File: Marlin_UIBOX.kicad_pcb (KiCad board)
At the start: 2 copper layers, 45 x 40 mm, 11 parts, among them J1 EXP1, J2 EXP2, J3 12864OLED_SPI, J4 SD_CARD, J5 ROT_ENCODER, Q1 2N3904

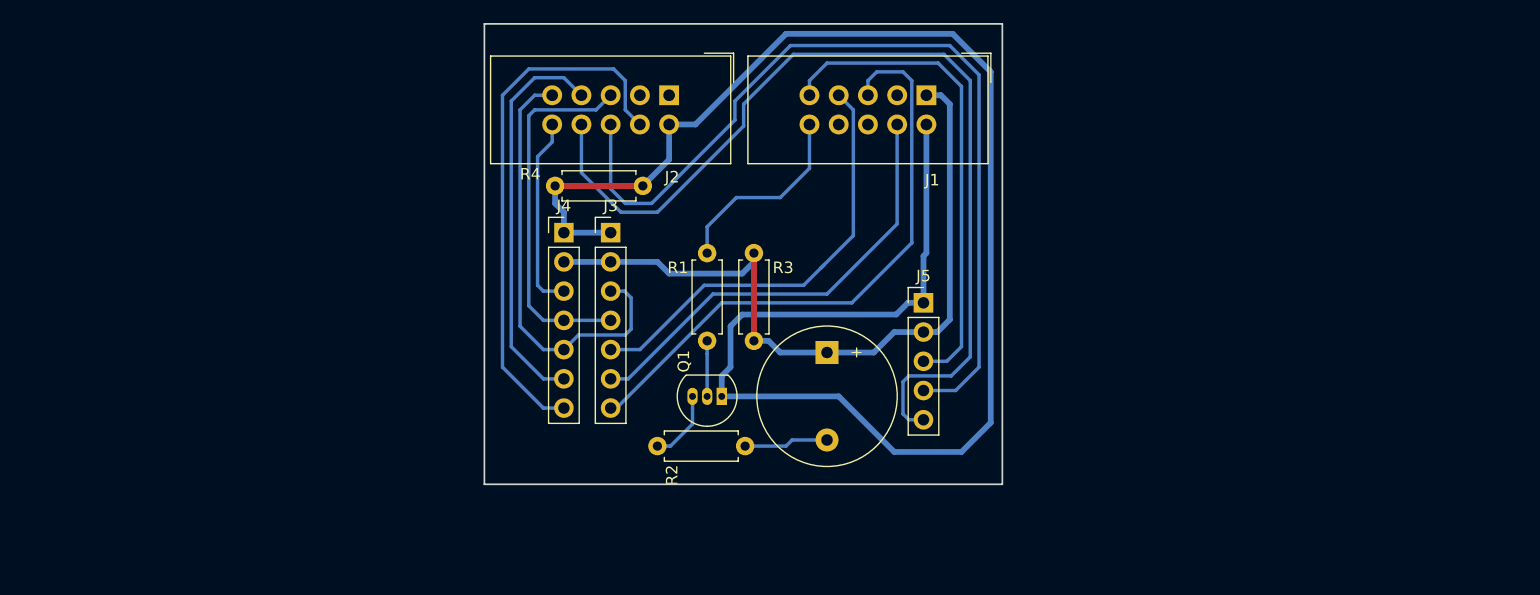
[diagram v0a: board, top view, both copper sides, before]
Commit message: PCB ver2 full board to board connections
* Complete re-do PCB to have PCB to PCB connectors no wire needed
* Went with 2 layer PCB instead of trying to make single layer...
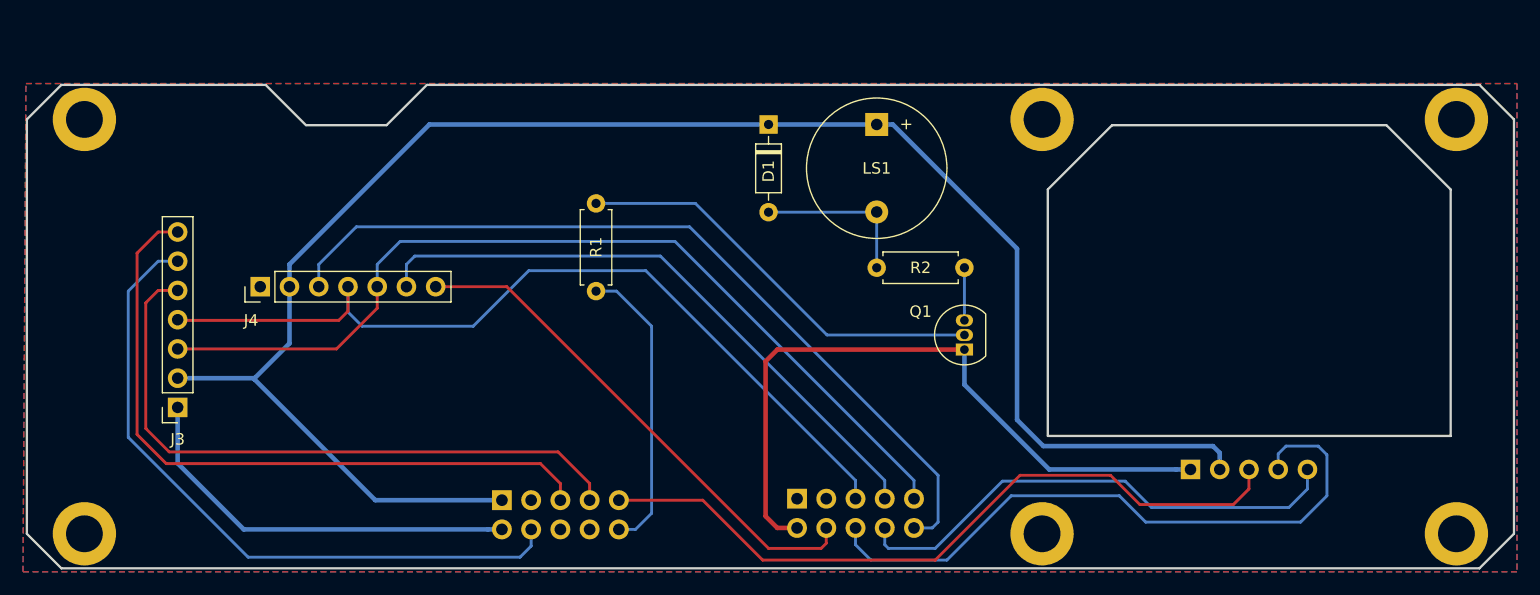
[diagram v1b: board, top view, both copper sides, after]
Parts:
- removed R3, R4: 0K, Resistors_ThroughHole:R_Axial_DIN0207_L6.3mm_D2.5mm_P7.62mm_Horizontal
- added D1: D, Diode_THT:D_DO-35_SOD27_P7.62mm_Horizontal, F.Cu at (154.7, 78.7)
- added REF**: MountingHole_3.2mm_M3_ISO14580_Pad, Mounting_Holes:MountingHole_3.2mm_M3_ISO14580_Pad, F.Cu at (214.4, 114.3)
- added REF**: MountingHole_3.2mm_M3_ISO14580_Pad, Mounting_Holes:MountingHole_3.2mm_M3_ISO14580_Pad, F.Cu at (214.4, 78.3)
- added REF**: MountingHole_3.2mm_M3_ISO14580_Pad, Mounting_Holes:MountingHole_3.2mm_M3_ISO14580_Pad, F.Cu at (178.4, 78.3)
- added REF**: MountingHole_3.2mm_M3_ISO14580_Pad, Mounting_Holes:MountingHole_3.2mm_M3_ISO14580_Pad, F.Cu at (178.4, 114.3)
- added REF**: MountingHole_3.2mm_M3_ISO14580_Pad, Mounting_Holes:MountingHole_3.2mm_M3_ISO14580_Pad, F.Cu at (95.2, 114.3)
- added REF**: MountingHole_3.2mm_M3_ISO14580_Pad, Mounting_Holes:MountingHole_3.2mm_M3_ISO14580_Pad, F.Cu at (95.2, 78.3)
- J1, J2: moved to B.Cu
- J3: footprint Pin_Headers:Pin_Header_Straight_1x07_Pitch2.54mm -> Connector_PinSocket_2.54mm:PinSocket_1x07_P2.54mm_Vertical
- J5: footprint Pin_Headers:Pin_Header_Straight_1x05_Pitch2.54mm -> Connector_PinSocket_2.54mm:PinSocket_1x05_P2.54mm_Vertical; moved to B.Cu
- LS1: footprint Buzzers_Beepers:Buzzer_12x9.5RM7.6 -> Buzzer_Beeper:Buzzer_12x9.5RM7.6
- Q1: footprint TO_SOT_Packages_THT:TO-92_Inline_Narrow_Oval -> Package_TO_SOT_THT:TO-92_Inline
- R1, R2: footprint Resistors_ThroughHole:R_Axial_DIN0207_L6.3mm_D2.5mm_P7.62mm_Horizontal -> Resistor_THT:R_Axial_DIN0207_L6.3mm_D2.5mm_P7.62mm_Horizontal
- moved J1 51.0 mm to (131.5, 111.4)
- moved J3 40.6 mm to (103.3, 103.3), turned to 180 degrees
- moved J2 36.8 mm to (157.2, 111.3)
- moved J5 27.3 mm to (191.3, 108.7), turned to 270 degrees
- moved J4 26.8 mm to (110.5, 92.8), turned to 90 degrees
- moved Q1 21.5 mm to (171.7, 98.3), turned to 90 degrees
- moved LS1 20.3 mm to (164.1, 78.7)
- moved R2 19.3 mm to (164.1, 91.2), turned to 0 degrees
- moved R1 10.2 mm to (139.7, 93.2), turned to 90 degrees
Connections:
- J1 pad 3: (no net) -> Net-(J1-Pad3)
- J1 pad 6: (no net) -> Net-(J1-Pad6)
- J1 pad 8: (no net) -> Net-(J1-Pad8)
- J2 pad 1: (no net) -> Net-(J2-Pad1)
- J2 pad 3: (no net) -> Net-(J2-Pad3)
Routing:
- net VCC: track 65.9 -> 151.6 mm
- net GND: track 151.4 -> 95.5 mm
- net /MISO: track 17.0 -> 72.4 mm
- net /MOSI: track 32.0 -> 75.2 mm
- net /SCK: track 38.1 -> 80.3 mm
- net /BT_EN2: track 82.7 -> 44.0 mm
- net Net-(Q1-Pad2): track 4.83 -> 36.7 mm
- net /BT_SW: track 42.4 -> 63.3 mm
- net /LCD_DC: track 39.1 -> 59.2 mm
- net /BT_EN1: track 76.9 -> 56.9 mm
- net /SD_SS: track 34.6 -> 53.5 mm
- net /LCD_RES: track 38.3 -> 56.1 mm
- net /BEEPER: track 17.1 -> 25.8 mm
- net /LCD_CS: track 51.9 -> 60.0 mm
- net Net-(D1-Pad2): track 7.33 -> 14.3 mm
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- added copper zone on B.Cu, net GND
- added copper zone on F.Cu, net GND
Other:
- board size 45 x 40 mm -> 129.2 x 42 mm
- net class Default: trace_width 0.3 -> 0.25
- net class POWER removed
- net class Power added: clearance 0.2, trace_width 0.4, via_dia 0.8, via_drill 0.4

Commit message: Move parts to fit both Replicator 1 and 2
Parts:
- moved D1 28.6 mm to (126.5, 83.3), turned to 0 degrees
- moved R2 9.76 mm to (171.7, 85.1), turned to 270 degrees
- moved LS1 6.19 mm to (162.1, 84.6)
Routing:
- net Net-(D1-Pad2): track 14.3 -> 45.1 mm
- net VCC: track 151.6 -> 156.3 mm
- net Net-(Q1-Pad3): track 4.57 -> 3.05 mm

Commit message: More tweaking
More tweaking
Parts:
- moved Q1 3.05 mm to (168.7, 98.3)
- moved R2 3.05 mm to (168.7, 85.1)
- moved J1 2.34 mm to (133.9, 111.3)
- moved LS1 2.29 mm to (159.8, 84.6)
- moved J2 0.95 mm to (156.2, 111.3)
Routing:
- net GND: track 95.5 -> 67.7 mm
- net /LCD_CS: track 60.0 -> 63.2 mm
- net Net-(Q1-Pad2): track 36.7 -> 33.7 mm
- net /LCD_RES: track 56.1 -> 59.0 mm
- net Net-(D1-Pad2): track 45.1 -> 42.5 mm
- net VCC: track 156.3 -> 158.9 mm
- net /LCD_DC: track 59.2 -> 61.7 mm
- net /BT_SW: track 63.3 -> 61.0 mm
- net /BT_EN1: track 56.9 -> 58.7 mm
- net /SCK: track 80.3 -> 81.3 mm
- net /BT_EN2: track 44.0 -> 45.0 mm
- net /SD_SS: track 53.5 -> 54.1 mm
- net /SD_DET: track 44.9 -> 44.3 mm
- net /BEEPER: track 25.8 -> 26.3 mm
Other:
- outline, holes or cut-outs redrawn

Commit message: This is the v1 that was fabricated by board house
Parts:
- REF** (x6): value MountingHole_3.2mm_M3_ISO14580_Pad -> MountingHole_3.2mm_M3; footprint Mounting_Holes:MountingHole_3.2mm_M3_ISO14580_Pad -> MountingHole:MountingHole_3.2mm_M3
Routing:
- net VCC: track 158.9 -> 159.7 mm
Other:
- outline, holes or cut-outs redrawn

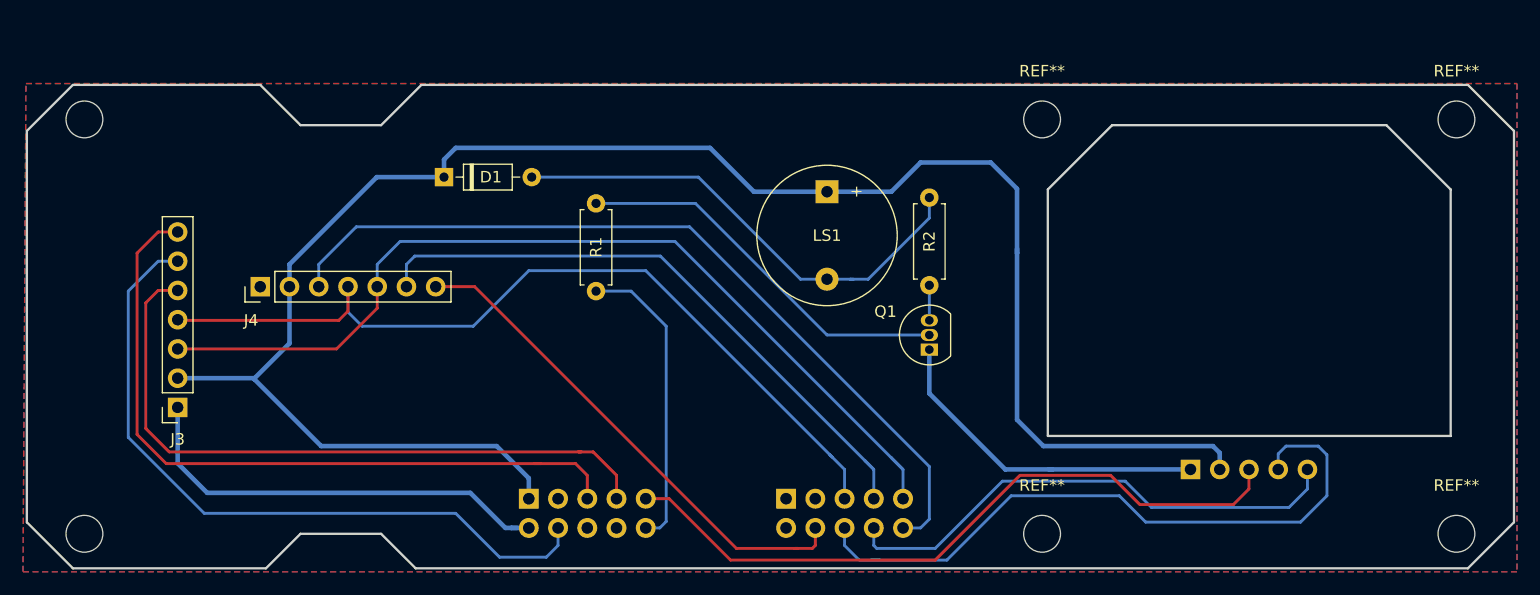
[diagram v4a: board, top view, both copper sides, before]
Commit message: Added second header for second position on SD card pcb
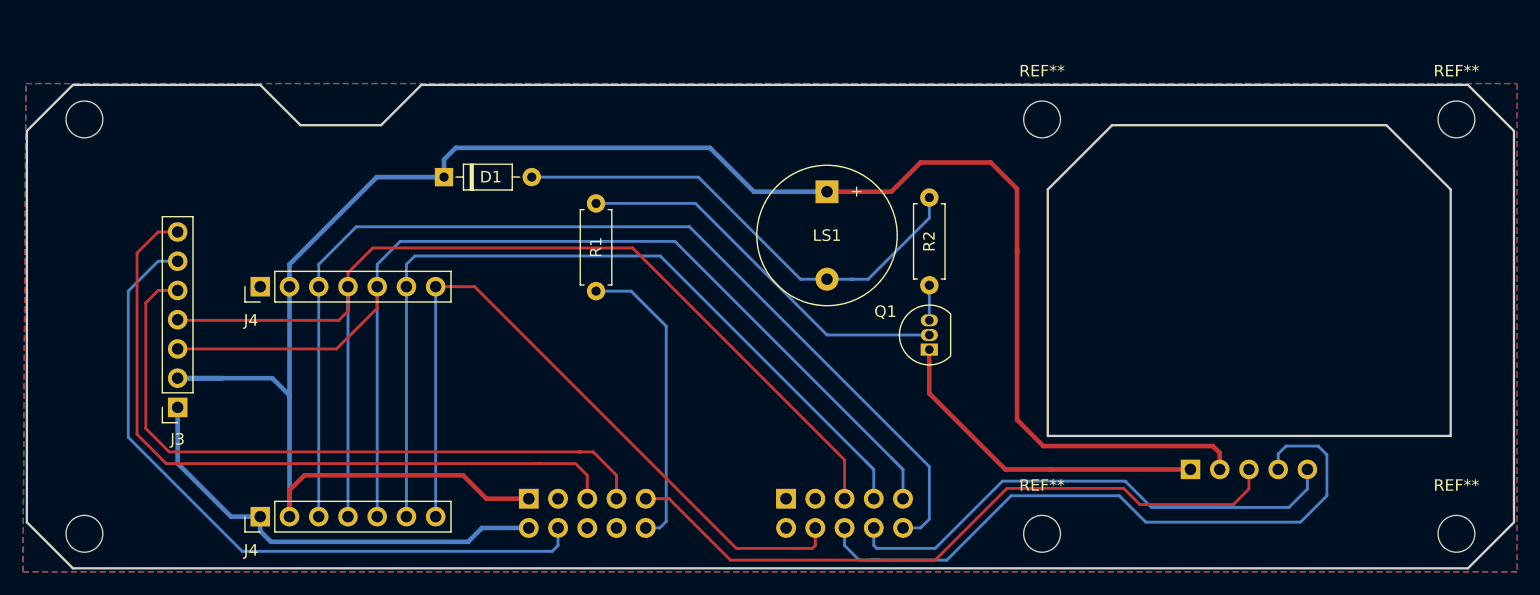
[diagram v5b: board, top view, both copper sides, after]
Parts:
- added J4: SD_CARD, Pin_Headers:Pin_Header_Straight_1x07_Pitch2.54mm, F.Cu at (110.5, 112.8)
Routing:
- net /MOSI: track 75.1 -> 95.7 mm
- net /SD_DET: track 44.3 -> 64.3 mm
- net /SD_SS: track 54.1 -> 74.1 mm
- net /MISO: track 72.1 -> 92.1 mm
- net /SCK: track 81.3 -> 101.2 mm
- net VCC: track 159.7 -> 173.2 mm
- net GND: track 67.7 -> 68.9 mm
- net /BT_SW: track 61.0 -> 60.0 mm
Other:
- outline, holes or cut-outs redrawn

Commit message: Added 3.3V Reg for LCD
* Added 3.3V Reg for LCD
* Added optional pull up resistors for LCD
* Added series resistors fro SPI signal for LCD to help with over/under
shoot
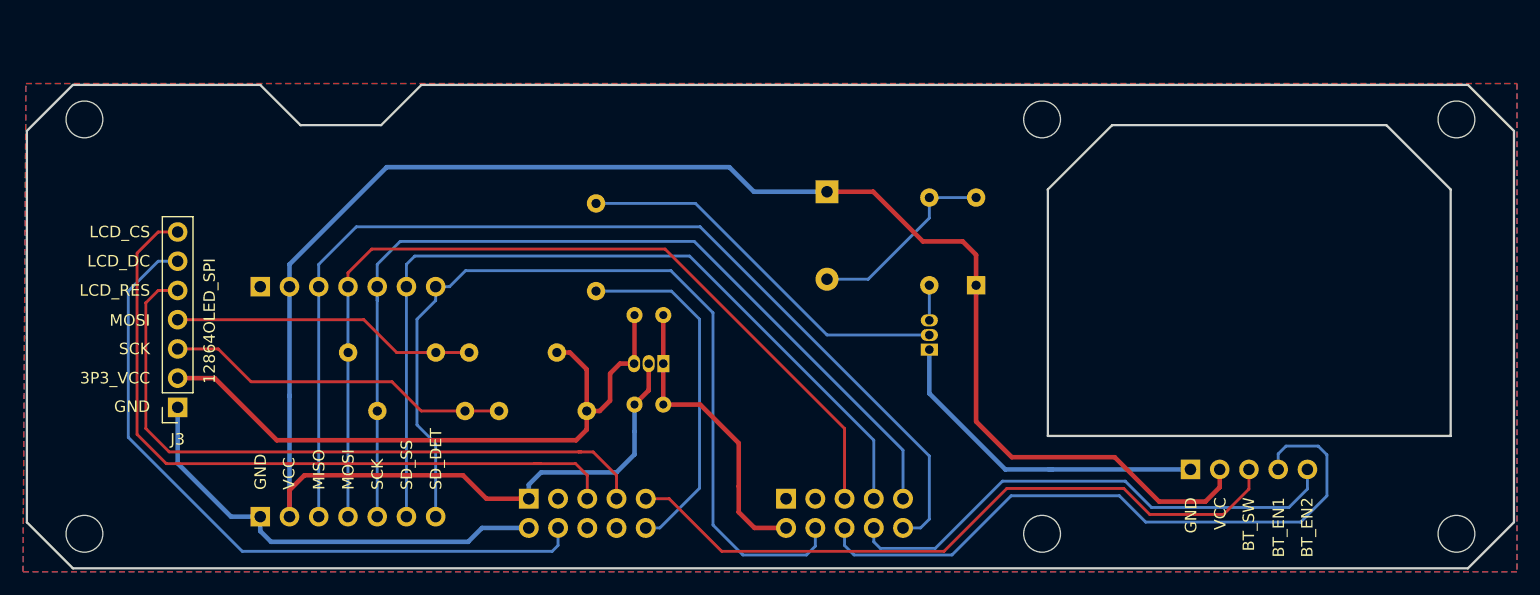
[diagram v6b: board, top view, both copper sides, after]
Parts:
- added C1: 1uf, Capacitor_THT:C_Rect_L4.6mm_W2.0mm_P2.50mm_MKS02_FKP02, B.Cu at (143.0, 103.1)
- added C2: 1uf, Capacitor_THT:C_Rect_L4.6mm_W2.0mm_P2.50mm_MKS02_FKP02, B.Cu at (143.0, 95.3)
- added R3: 2.2K, Resistor_THT:R_Axial_DIN0207_L6.3mm_D2.5mm_P7.62mm_Horizontal, B.Cu at (136.3, 98.6)
- added R4: 2.2K, Resistor_THT:R_Axial_DIN0207_L6.3mm_D2.5mm_P7.62mm_Horizontal, B.Cu at (138.9, 103.6)
- added R5: 1K, Resistor_THT:R_Axial_DIN0207_L6.3mm_D2.5mm_P7.62mm_Horizontal, B.Cu at (120.7, 103.6)
- added R6: 1K, Resistor_THT:R_Axial_DIN0207_L6.3mm_D2.5mm_P7.62mm_Horizontal, B.Cu at (118.2, 98.6)
- added U1: MCP1700-3302E_TO92, Package_TO_SOT_THT:TO-92_Inline, B.Cu at (145.5, 99.5)
- D1, J4 (x2), LS1, Q1, R1, R2: moved to B.Cu
- moved D1 47.2 mm to (172.7, 92.7), turned to 90 degrees
- turned J4 to 270 degrees (x2)
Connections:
- J3 pad 2: VCC -> /3P3_VCC
- J3 pad 3: /SCK -> /LCD_SCK
- J3 pad 4: /MOSI -> /LCD_MOSI
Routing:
- net /3P3_VCC: track 0.00 -> 58.0 mm
- net /LCD_SCK: track 0.00 -> 30.2 mm
- net /LCD_MOSI: track 0.00 -> 26.6 mm
- net GND: track 68.9 -> 95.3 mm
- net Net-(D1-Pad2): track 42.5 -> 16.9 mm
- net /SCK: track 101.2 -> 81.4 mm
- net /MOSI: track 95.7 -> 77.8 mm
- net /SD_DET: track 64.3 -> 77.8 mm
- net /BEEPER: track 26.3 -> 30.8 mm
- net /BT_EN1: track 58.7 -> 57.5 mm
- net /MISO: track 92.1 -> 92.7 mm
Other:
- board text added: "3P3_VCC"
- board text added: "BT_EN1"
- board text added: "BT_EN2"
- board text added: "BT_SW"
- board text added: "GND"
- board text added: "LCD_CS"
- board text added: "LCD_DC"
- board text added: "LCD_RES"
- board text added: "MISO"
- board text added: "MOSI"
- board text added: "Marlin_UIBOX v4"
- board text added: "SCK"
- board text added: "SD_DET"
- board text added: "SD_SS"
- board text added: "VCC"
